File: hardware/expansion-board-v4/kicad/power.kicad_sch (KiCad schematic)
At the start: 40 parts, among them J9 MX1.25WT-2P BAT, SW3 TS24CA, U1 ME6211C33M5, U18 CH224K, U19 SY6970, U2 TPS7A2033PDBVR, U20 SY7069, U3 TPS7A2033PDBVR

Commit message: hardware(v4.7): 修正 C99 并刷新整套制造与装配文件
在用户修订的布局上将 C99 改为 100nF/0402，复用 C37/C52 的 C307331；同步原理图版本、BOM/CPL、装配图、安装助手及制造归档，更新下单入口和未决电气项。

验证：DRC 0 违规/0 未连通，存盘覆铜与包源一致性已核对；提交前版本包/安装助手20项，18通过、2跳过。元件契约中已记录的 C84 两条子断言失败按用户范围保留；Y4 供电和 U22 VREF 建议尚待闭环。内部工具、审计报告和采购过程文件按仓库规则仅留本地。
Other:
- title: Expansion Board V1 - Power: 5V in, 3x LDO -> Expansion Board V4.7 - Power: 5V in, 3x LDO
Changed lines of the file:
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@@
 	(paper "A3")
 	(title_block
-		(title "Expansion Board V1 - Power: 5V in, 3x LDO")
+		(title "Expansion Board V4.7 - Power: 5V in, 3x LDO")
 		(date "2026-08-01")
-		(rev "V1")
+		(rev "V4.7")
 		(company "Pilot Kit")
 	)

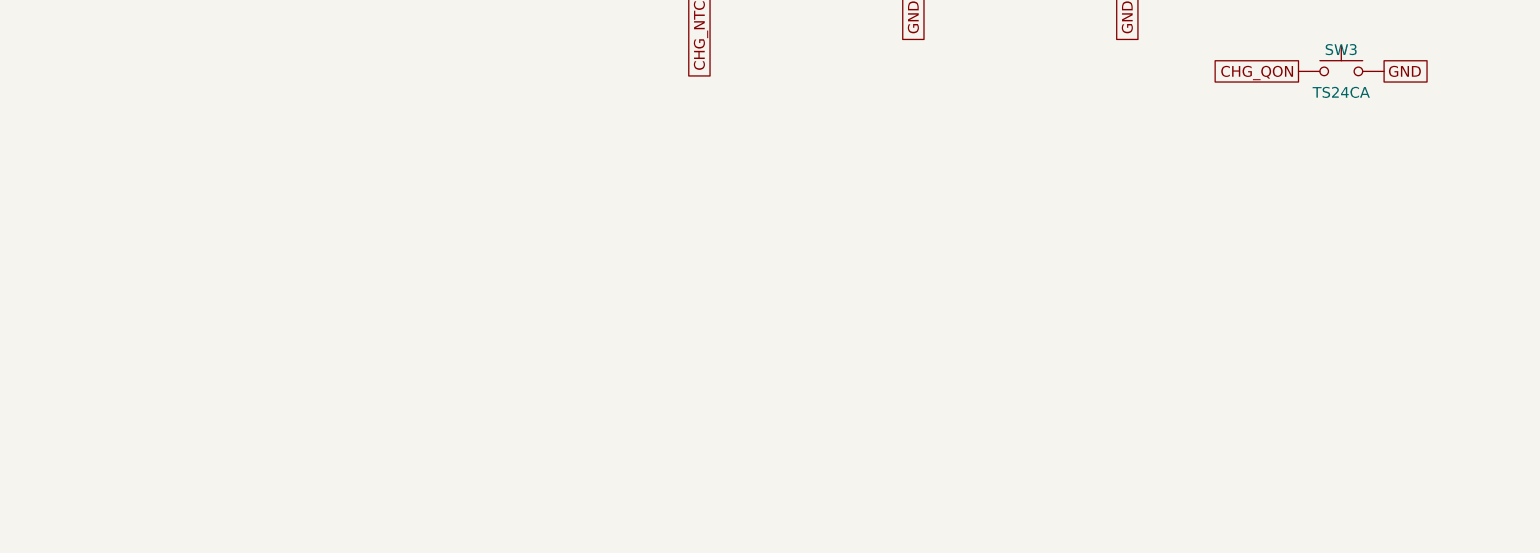
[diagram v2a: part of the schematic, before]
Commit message: hardware(v4.8): GNSS 模块 VBAT 常供电，开机不再冷启动
板上那颗 ATGM336H 本身就有 RTC（6N 手册 §2.4：pin6 VBAT = "RTC 及 SRAM 后备
电源"），但 pin6 一直接在 3V3_GNSS 上——与模块主供电同一条轨，关机
(BATFET_DIS) 时一起断电。于是模块每次开机都从零冷启动：既没有时间，也没有
星历。这同时是「开机没有时间」的硬件根因，和 gps_task.c 里 "gps-coarse" 粗校
兜底一直走不到的原因。

方案成立的前提先做了实机验证：室外定位后拔掉天线，让模块彻底失锁
(fix=0 sats=0 snr=0)，RMC 的时间字段仍逐秒前进 —— 模块的 RTC 确实独立于定位
在走。所以不需要外挂 RTC 芯片，板上已经有一颗，缺的只是一路不断电的 VBAT。

电路（6 件，取电点是 BAT_P：关机断的是 BAT→SYS，BAT_P 这侧照常带电）
    BAT_P ─[U23 TPS7A2033]─ 3V3_BKP ─[D7]─┬─ GNSS_VBAT ─ U7.pin6
                                          └─[R63 2.2k]─ BT1(+)
    C101/C102 = U23 的输入/输出去耦

  · U23 复用已采购料号 C2862740（BOM 用量 2→3），IGND 典型 6.5µA；
    加 GNSS 的 Ibat 10µA，总账约 17µA —— 对 5000mAh 是 33 年量级
  · D7 不能省：TPS7A20 手册写明输入掉电时电流会从 OUT 倒灌回 IN 并可能损坏
    器件。主电池被保护板切断后 BAT_P=0，没有它电池就会经 LDO 往回灌
  · BT1 = Seiko MS621FE-FL11E 焊接式可充电锂锰，5.5mAh，充到 2.91V 约 75%
    → 续航约 17 天。⚠️ 只能用 ML/MS 体系，**LIR 系列满电 4.2V 会超 Vbat 极限 3.6V**
  · 中途曾设计成「带线 CR2032 + 座子」（先 PH2.0 后 SH1.0），焊接式把座子和
    一颗 OR-ing 二极管一起省掉，"4.2V 主电池插错备份口"这条失效路径也随之消失

自建封装与 3D 模型（KiCad 官方库那个用不了）
  官方库有同名的 BatteryHolder_Seiko_MS621F，但它焊盘中心距 1.5mm，而
  FL11E 实际是 2.5mm，差 1mm 焊不上 —— 同一颗电池不同端子后缀
  （FL11E / FL01E / FE11E）焊脚并不通用，跟 J9 栽的是同一类坑。
  封装按 SII 官方样本 MicroBattery_E_20230330_rev05 第 14 页 1:1 建立。
  .wrl 里的圆柱必须用 IndexedFaceSet 显式建面：用 VRML 的 Cylinder 图元时
  整个元件都不显示（连焊脚的 Box 一起没），KiCad 静默忽略、不报错。

两个 DRC 抓不到的坑
  1) U7.pin6 改网络时必须连旧走线一起摘。焊盘改了网络而压在它上面的 4 段
     3V3_GNSS 铜不动，两个网络就被直接短在一起、二极管被旁路，而 DRC 只会
     报"未连通"不会报"短路"——它们确实是连着的。
  2) BT1 初版摆在 (142,107)，与 M2.5 安装孔 H4 实际重叠 2.39mm，DRC 全程
     0 违例：孔挂 F 面、电池在 B 面，按层查 courtyard 两边各自合规，但螺丝
     是贯穿的。重新求解时把四个贯穿孔一并当障碍，现落点 (140,76.4)，
     距投影区 +4.10 / 距板右边 +4.60 / 最近障碍 +14.26。

布线由用户手工完成并 review 通过：缺线 0 / 孤立断头铜 0 / 焊盘未接覆铜 0 /
铜层 DRC 0 / 丝印 DRC 0 / In1 参考面完整。BKP_CELL 走线 0.15mm 宽、68.9mm 长，
按 IPC-2221 载流约 0.6A 而实际电流 0.4mA，线阻 0.23Ω 相对串联的 R63=2.2k
占 0.01% —— 线宽不是约束，这条路的限流本来就由 R63 决定。

动了三处门禁（都说明理由）
  · test_board_revision_contract: 目标版本 V4.7 → V4.8（版本跟随）
  · test_v4_placement_contract / test_component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
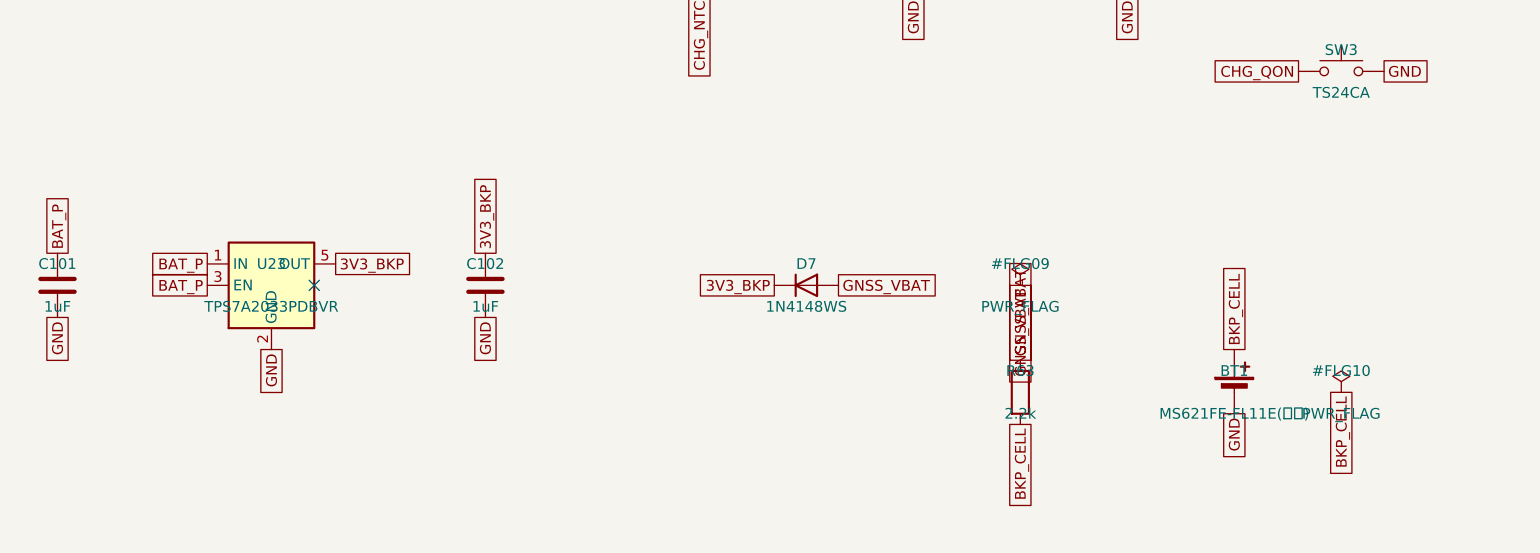
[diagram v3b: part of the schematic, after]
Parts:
- added BT1: MS621FE-FL11E(选贴), expansion-board-v4:MS621FE-FL11E, symbol Device:Battery_Cell
- added C101, C102: 1uF, Capacitor_SMD:C_0603_1608Metric, symbol Device:C
- added D7: 1N4148WS, Diode_SMD:D_SOD-323, symbol Device:D
- added R63: 2.2k, Resistor_SMD:R_0603_1608Metric, symbol Device:R
- added U23: TPS7A2033PDBVR, Package_TO_SOT_SMD:SOT-23-5, symbol Regulator_Linear:TPS7A20xxxDBV
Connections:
- net BAT_P: now also C101.1, U23.1 (IN), U23.3 (EN)
- net GND: now also BT1.2 (-), C101.2, C102.2, U23.2 (GND)
- new net 3V3_BKP: C102.1, D7.1 (K), U23.5 (OUT)
- new net BKP_CELL: BT1.1 (+), R63.2
- new net GNSS_VBAT: D7.2 (A), R63.1
- no-connect marks 9 -> 10
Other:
- title: Expansion Board V4.7 - Power: 5V in, 3x LDO -> Expansion Board V4.8 - Power: 5V in, 3x LDO

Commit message: hardware(v4.8): 修独立审计的 4 项，其中两项是设计错误
另一路 agent 的投产前独立审计报了 4 项，逐条核实**全部成立**，前两项是我的错。

① P1 — D7 极性接反（会让整条备份供电失效）
   KiCad 的 Device:D 符号是 **pin1=K(阴极) / pin2=A(阳极)**，我按"pin1 是阳极"
   的想当然写了 {"1":"3V3_BKP","2":"GNSS_VBAT"}，阳极落在了 GNSS_VBAT 侧。
   后果：U23 供不了电、BT1 充不上，而**DRC/ERC 都查不出极性方向**——网络连接
   完全"正确"，只是二极管装反了。注释里我写的明明是"阳极接 3V3_BKP"，落到
   代码时没去查符号定义。

   修法取了个巧：原理图交换引脚网络 + PCB 上 D7 旋转 180°。两个焊盘的物理位置
   随之互换，(80.874,88.324) 仍是 3V3_BKP、(80.874,86.224) 仍是 GNSS_VBAT，
   **走线一段都不用动**，而实物极性方向正过来了。

② P2 — BT1 焊盘中心距做成 2.5mm，官方是 1.5mm
   官方尺寸图标的是 `0.5 / 2 / 0.5`，那个 2 是**外缘到外缘**（1.5 中心距 +
   0.5 一条焊脚宽 = 2.0），我读成了内缘间距，于是算出 2.5。
   独立验算坐实：底视图按 φ6.8=472px 反算，两焊脚中心距 100px = 1.44mm、
   焊脚宽 36px = 0.52mm（官方标 0.5，比例尺自洽）。

   这也意味着**我当初否定 KiCad 官方封装的理由完全不成立**——它的 1.5mm 一直
   是对的。保留自建封装只是为了带自己的 3D 模型和这段记录，描述已改正。

   连带修掉的：3D 模型焊脚位置同步 ±1.25→±0.75；重放 BT1 时我漏了原朝向
   （-90°）导致焊盘跑到另一侧，补回后两条走线各差 0.5mm，已接上；焊盘移动后
   压到 GND 覆铜（clearance + solder_mask_bridge），重灌覆铜解决；丝印圆
   R3.65 压在焊盘开窗上，收到 R3.05（焊盘内缘 3.2 以内）；D7 位号旋转后与
   C101/U7.pad5 相撞，已重新安置。

③ P1 — 下单入口仍指向 V4.7
   release/README.md 标题、两个包链接、SHA256，以及 internal/下单说明.md 的
   四处引用，全部改指 V4.8 并重算校验值。照旧文档下单会拿到没有备份供电的板。

④ P2 — 选择性贴装规则未同步
   SELECTIVE_PLACEMENT 的「电源部分」名单漏了新增 6 件（中英文都漏），
   计数 29→35。**这是同一个陷阱第三次出现**：gen_assembly_web.py 的
   POWER_SECTION 上一轮刚补过，这次轮到手写文档。它们全部吊在 BAT_P 上，
   不带电源版不贴 U19/J9 时必须跟着不贴，否则 U23 输入悬空、整组失效而板子
   照常工作。

修复后板子状态
   缺线 0 / 孤立断头铜 0 / 焊盘未接覆铜 0
   铜层 DRC **0 违例** / 丝印 DRC **0 违例**
   走线 1849 段 / 过孔 492
   D7 电流方向 3V3_BKP → GNSS_VBAT ✓   BT1 焊盘中心距 1.50mm ✓

全部产物按修复后的板重出：ROUTES/PLACEMENT/ZONES/SILK、BOM、装配文档、
CHECKLIST、SMT 三变体、render、Gerber 与源码包（旧包留档在
build/pre-audit-fix-release/）、装配助手数据。

门禁：V4 全绿；遗留 4 项均为 expansion-board-v3 既存失败。
⚠️ check_gerber.py 仍未跑（缺 gerbonara），274X 格式与原点参数无替代验证。
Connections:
- net 3V3_BKP: now also D7.2 (A); no longer D7.1 (K)
- net GNSS_VBAT: now also D7.1 (K); no longer D7.2 (A)
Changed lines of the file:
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@@
 		)
 	)
-	(global_label "3V3_BKP"
+	(global_label "GNSS_VBAT"
 		(shape passive)
 		(at 135.89 241.3 180)
 		(effects (font (size 1.27 1.27)) (justify right))
 	)
-	(global_label "GNSS_VBAT"
+	(global_label "3V3_BKP"
 		(shape passive)
 		(at 143.51 241.3 0)

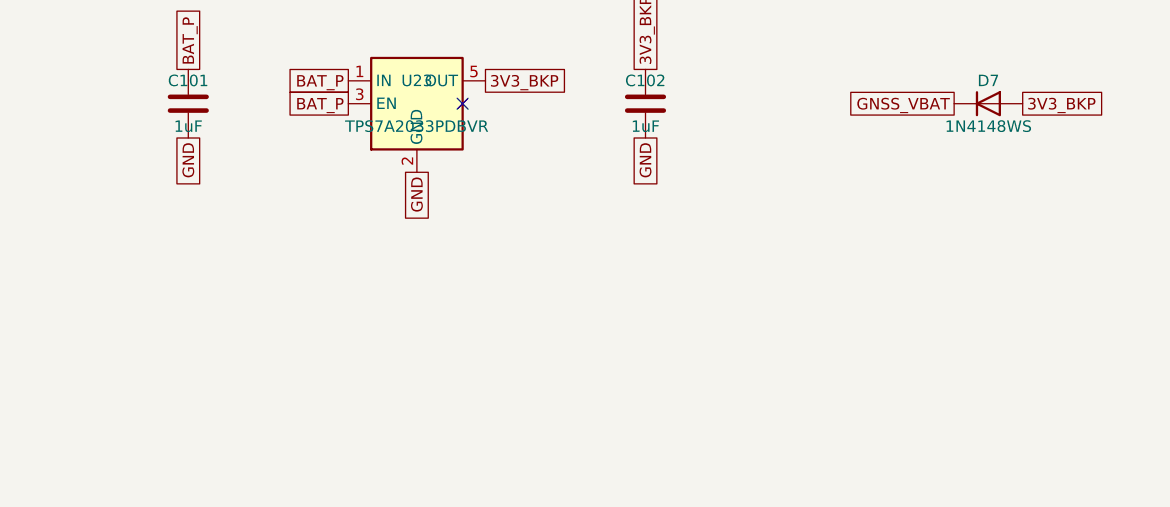
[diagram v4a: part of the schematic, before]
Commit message: hardware(v4.8): 加电源/充电指示灯 D8/D9，丝印回丝印层，电源选贴名单四处对齐
## 加了什么

全板此前**一颗 LED 都没有**（D2~D6 是 ESD 管、D7 是备份供电二极管），
上电后没有任何不拆机可见的状态。

    D8 + R64   电源灯   3V3_DIG → LED → 1k → GND，上电即亮、关机自灭
    D9 + R65   充电灯   3V3_DIG → LED → 1k → CHG_STAT

CHG_STAT 原本是条**死信号**：SY6970 的 STAT(pin4) 开漏输出 + R45 10k 上拉，
全板没有任何消费者。手册特性栏原文 "Charge Status Outputs for LED or Host"，
直驱 LED 就是设计用途。接上等于把它救活，且**不占任何 GPIO**——
充电中亮（STAT ≤0.4V）、充满灭（高阻被 R45 拉到 3V3，两端无压差）、
**充电故障 1Hz 闪**（手册原文，白捡一个故障指示）。

限流都用 1k 复用板上已有料号，不新增 SMT 上料种类；取 ~1mA 而非额定 20mA。

⚠️ 只能用 **Vf 2.0~2.2V** 档（红/黄/橙/普绿）。维护者那批样品包里的
蓝(467-470nm)、翠绿(520-523)、白 是 **3.0~3.1V**，挂 3.3V 轨上点不亮——
充电灯还要再扣 STAT 的 0.4V，只剩 0.2V，连正向导通都不够。
所以 value 锁 Vf 档不锁颜色，颜色手焊时挑。D8/D9 自备料、无嘉立创料号，
和 BT1 一样不进任何 CPL，需手焊。

## 丝印：位号一律留丝印层（维护者纠正）

我一度把 D8/D9/R64/R65/SW3 五个位号搬到 **F.Fab** 来消除 14 项丝印 DRC 违例。
维护者纠正：「你又把丝印放到 FFAB 了，**每次都这样**」。

搬 F.Fab 不是解决问题，是**把问题藏起来**——板面丝印是实物上唯一能直接读到
的位号，手焊/返修/现场排查都靠它，F.Fab 只存在于装配图 PDF 里。
当时那三条自辩全部不成立：维护者自己在 KiCad 里重排了一遍，五个位号
**全部回到 F.Silkscreen、字高 0.8mm，丝印 DRC 依然 0 违例**。

连带损失也暴露了：export_placement **只冻结丝印层的位号**（F.Fab 被它判为
"算法排不下"的失败状态，不予固化），所以那 5 个当场丢掉固化，
PLACEMENT.py 报「240 元件 / **235** 位号」。改回来后恢复 240/240。

维护者还加了两条板级功能标注 `PWR↓` / `CHG↓`（F.SilkS 0.8mm，箭头各指一灯）
——位号只说"这是个二极管"，这两条才说明它是干什么的。
门禁按 test_v4_placement_contract 自己的设计**单列** V48_LABELS，
没有把 FINALIZED_GRAPHICS_COUNT 基线 +1（那会让合同退化成事后追认）；
已做突变验证：数错一条会变红。

## 电源选贴名单：四处副本对齐

D9/R65 的阴极落在 U19 的 STAT 脚上，不带电源版没有 U19 就永远不亮，
必须随电源部分一起不贴。D8/R64 吃 3V3_DIG（U1 从 VCC_5V 降压），
两个版本都要贴，**不在此列**。

补登时发现这份名单在仓库里有**四处**同语义副本，而 2026-09-13 加 GNSS
备份供电那 6 件时**只登记了一处**：

    tools/gen_assembly_web.py           POWER_SECTION  ← 当时只改了这处
    internal/tools/gen_jlc_smt.py       VARIANT_PWR    ← 漏
    internal/tools/gen_assembly_pdf.py  VARIANT_PWR    ← 漏
    internal/tools/gen_place_xlsx.py    PWR_REFS       ← 漏

没暴露只因为 BUILD_VARIANT 一直是 "powered"，VARIANT_PWR 压根没参与计算。
四处现已一致（各 37 个位号，脚本核对过），并在每处写明另外三处在哪、
以及哪两处（gen_power_csv.WANT 采购口径 / gen_pcb.BACKSIDE B面集合）
语义不同不要跟着改。装配图的「电源区」随之从 29 → 37。

## 布线与丝印上踩到的

· 0805 竖放 c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
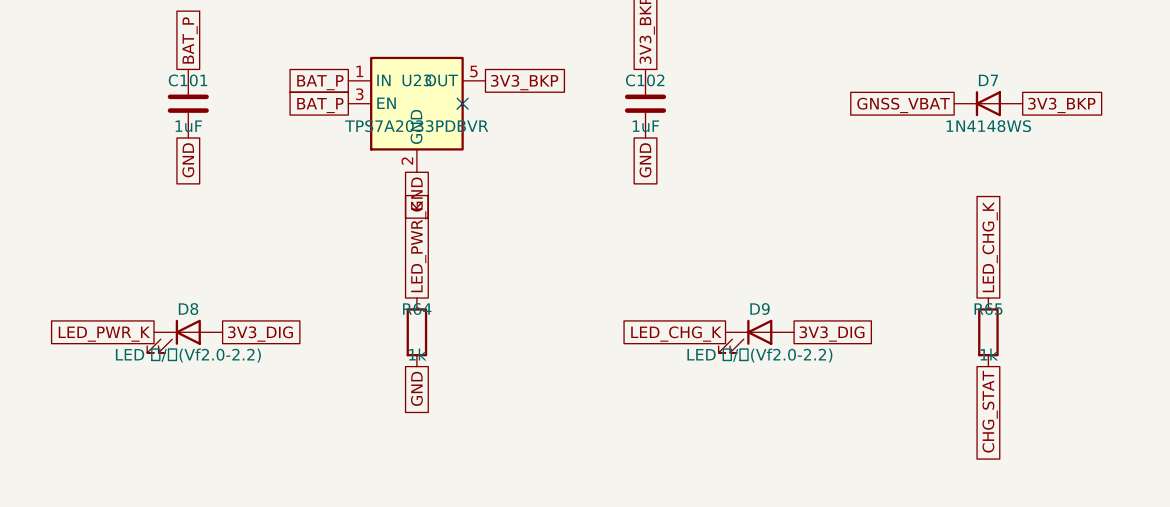
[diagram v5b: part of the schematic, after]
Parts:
- added D8, D9: LED 红/黄(Vf2.0-2.2), LED_SMD:LED_0805_2012Metric, symbol Device:LED
- added R64, R65: 1k, Resistor_SMD:R_0603_1608Metric, symbol Device:R
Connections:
- net 3V3_DIG: now also D8.2 (A), D9.2 (A)
- net CHG_STAT: now also R65.2
- net GND: now also R64.2
- new net LED_CHG_K: D9.1 (K), R65.1
- new net LED_PWR_K: D8.1 (K), R64.1
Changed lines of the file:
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@@
+		(effects (font (size 1.27 1.27)) (justify right))
+	)
+	(symbol
+		(lib_id "Device:LED")
+		(at 50.8 266.7 0)
+		(unit 1)
+		(exclude_from_sim no)
+		(in_bom yes)
+		(on_board yes)
+		(dnp no)
+		(property "Reference" "D8"
+			(at 50.8 264.16 0)
+			(effects (font (size 1.27 1.27)))
+		)
+		(property "Value" "LED 红/黄(Vf2.0-2.2)"
+			(at 50.8 269.24 0)
+			(effects (font (size 1.27 1.27)))
+		)
+		(property "Footprint" "LED_SMD:LED_0805_2012Metric"
+			(at 50.8 271.78 0)
+			(effects (font (size 1.27 1.27))
+				(hide yes))
+		)
+		(property "Datasheet" "~"
+			(at 50.8 274.32 0)
+			(effects (font (size 1.27 1.27))
+				(hide yes))
+		)
+		(pin "1"
+		)
+		(pin "2"
+		)
+		(instances
+			(project "expansion-board-v4"
+				(path "/10000000-0000-4000-8000-000000000001/20000000-0000-4000-8000-000000000001"
+					(reference "D8")
+					(unit 1)
+				)
+			)
+		)
+	)
+	(global_label "LED_PWR_K"
+		(shape passive)
+		(at 46.99 266.7 180)
+		(effects (font (size 1.27 1.27)) (justify right))
+	)
+	(global_label "3V3_DIG"
+		(shape passive)
+		(at 54.61 266.7 0)
+		(effects (font (size 1.27 1.27)) (justify left))
+	)
+	(symbol
+		(lib_id "Device:R")
+		(at 76.2 266.7 0)
+		(unit 1)
+		(exclude_from_sim no)
+		(in_bom yes)
+		(on_board yes)
+		(dnp no)
+		(property "Reference" "R64"
+			(at 76.2 264.16 0)
+			(effects (font (size 1.27 1.27)))
+		)
+		(property "Value" "1k"
+			(at 76.2 269.24 0)
+			(effects (font (size 1.27 1.27)))
+		)
+		(property "Footprint" "Resistor_SMD:R_0603_1608Metric"
+			(at 76.2 271.78 0)
+			(effects (font (size 1.27 1.27))
+				(hide yes))
+		)
+		(property "Datasheet" "~"
+			(at 76.2 274.32 0)
+			(effects (font (size 1.27 1.27))
+				(hide yes))
+		)
+		(pin "1"
+		)
+		(pin "2"
+		)
+		(instances
+			(project "expansion-board-v4"
+				(path "/10000000-0000-4000-8000-000000000001/20000000-0000-4000-8000-000000000001"
+					(reference "R64")
+					(unit 1)
+				)
+			)
+		)
+	)
+	(global_label "LED_PWR_K"
+		(shape passive)
+		(at 76.2 262.89 270)
+		(effects (font (size 1.27 1.27)) (justify left))
+	)
+	(global_label "GND"
+		(shape passive)
+		(at 76.2 270.51 90)
+		(effects (font (size 1.27 1.27)) (justify right))
+	)
+	(symbol
+		(lib_id "Device:LED")
+		(at 114.3 266.7 0)
+		(unit 1)
+		(exclude_from_sim no)
+		(in_bom yes)
+		(on_board yes)
+		(dnp no)
+		(property "Reference" "D9"
+			(at 114.3 264.16 0)
+			(effects (font (size 1.27 1.27)))
+		)
+		(property "Value" "LED 红/黄(Vf2.0-2.2)"
+			(at 114.3 269.24 0)
+			(effects (font (size 1.27 1.27)))
+		)
+		(property "Footprint" "LED_SMD:LED_0805_2012Metric"
+			(at 114.3 271.78 0)
+			(effects (font (size 1.27 1.27))
+				(hide yes))
+		)
+		(property "Datasheet" "~"
+			(at 114.3 274.32 0)
+			(effects (font (size 1.27 1.27))
+				(hide yes))
+		)
+		(pin "1"
+		)
+		(pin "2"
+		)
+		(instances
+			(project "expansion-board-v4"
+				(path "/10000000-0000-4000-8000-000000000001/20000000-0000-4000-8000-000000000001"
+					(reference "D9")
+					(unit 1)
+				)
+			)
+		)
+	)
+	(global_label "LED_CHG_K"
+		(shape passive)
+		(at 110.49 266.7 180)
+		(effects (font (size 1.27 1.27)) (justify right))
+	)
+	(global_label "3V3_DIG"
+		(shape passive)
+		(at 118.11 266.7 0)
+		(effects (font (size 1.27 1.27)) (justify left))
+	)
+	(symbol
+		(lib_id "Device:R")
+		(at 139.7 266.7 0)
+		(unit 1)
+		(exclude_from_sim no)
+		(in_bom yes)
+		(on_board yes)
+		(dnp no)
+		(property "Reference" "R65"
+			(at 139.7 264.16 0)
+			(effects (font (size 1.27 1.27)))
+		)
+		(property "Value" "1k"
+			(at 139.7 269.24 0)
+			(effects (font (size 1.27 1.27)))
+		)
+		(property "Footprint" "Resistor_SMD:R_0603_1608Metric"
+			(at 139.7 271.78 0)
+			(effects (font (size 1.27 1.27))
+				(hide yes))
+		)
+		(property "Datasheet" "~"
+			(at 139.7 274.32 0)
+			(effects (font (size 1.27 1.27))
+				(hide yes))
+		)
+		(pin "1"
+		)
+		(pin "2"
+		)
+		(instances
+			(project "expansion-board-v4"
+				(path "/10000000-0000-4000-8000-000000000001/20000000-0000-4000-8000-000000000001"
+					(reference "R65")
+					(unit 1)
+				)
+			)
+		)
+	)
+	(global_label "LED_CHG_K"
+		(shape passive)
+		(at 139.7 262.89 270)
+		(effects (font (size 1.27 1.27)) (justify left))
+	)
+	(global_label "CHG_STAT"
+		(shape passive)
+		(at 139.7 270.51 90)
 		(effects (font (size 1.27 1.27)) (justify right))
 	)

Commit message: feat(v4.11): 固化扩展板并修正电池补偿
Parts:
- added D10: 1N4148WS, Diode_SMD:D_SOD-323, symbol Device:D
- added R67: 1k, Resistor_SMD:R_0603_1608Metric, symbol Device:R
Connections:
- net CHG_QON: now also D10.1 (K)
- new net P4_GPIO4_SW3_SENSE: R67.1
- new net SW3_SENSE_A: D10.2 (A), R67.2
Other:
- title: Expansion Board V4.8 - Power: 5V in, 3x LDO -> Expansion Board V4.11 - Power: 5V in, 3x LDO
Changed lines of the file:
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@@
 	(paper "A3")
 	(title_block
-		(title "Expansion Board V4.8 - Power: 5V in, 3x LDO")
+		(title "Expansion Board V4.11 - Power: 5V in, 3x LDO")
 		(date "2026-08-01")
-		(rev "V4.8")
+		(rev "V4.11")
 		(company "Pilot Kit")
 	)
@@
 		(effects (font (size 1.27 1.27)) (justify left))
 	)
+	(symbol
+		(lib_id "Device:R")
+		(at 228.6 215.9 0)
+		(unit 1)
+		(exclude_from_sim no)
+		(in_bom yes)
+		(on_board yes)
+		(dnp no)
+		(property "Reference" "R67"
+			(at 228.6 213.36 0)
+			(effects (font (size 1.27 1.27)))
+		)
+		(property "Value" "1k"
+			(at 228.6 218.44 0)
+			(effects (font (size 1.27 1.27)))
+		)
+		(property "Footprint" "Resistor_SMD:R_0603_1608Metric"
+			(at 228.6 220.98 0)
+			(effects (font (size 1.27 1.27))
+				(hide yes))
+		)
+		(property "Datasheet" "~"
+			(at 228.6 223.52 0)
+			(effects (font (size 1.27 1.27))
+				(hide yes))
+		)
+		(pin "1"
+		)
+		(pin "2"
+		)
+		(instances
+			(project "expansion-board-v4"
+				(path "/10000000-0000-4000-8000-000000000001/20000000-0000-4000-8000-000000000001"
+					(reference "R67")
+					(unit 1)
+				)
+			)
+		)
+	)
+	(global_label "P4_GPIO4_SW3_SENSE"
+		(shape passive)
+		(at 228.6 212.09 270)
+		(effects (font (size 1.27 1.27)) (justify left))
+	)
+	(global_label "SW3_SENSE_A"
+		(shape passive)
+		(at 228.6 219.71 90)
+		(effects (font (size 1.27 1.27)) (justify right))
+	)
+	(symbol
+		(lib_id "Device:D")
+		(at 254 215.9 0)
+		(unit 1)
+		(exclude_from_sim no)
+		(in_bom yes)
+		(on_board yes)
+		(dnp no)
+		(property "Reference" "D10"
+			(at 254 213.36 0)
+			(effects (font (size 1.27 1.27)))
+		)
+		(property "Value" "1N4148WS"
+			(at 254 218.44 0)
+			(effects (font (size 1.27 1.27)))
+		)
+		(property "Footprint" "Diode_SMD:D_SOD-323"
+			(at 254 220.98 0)
+			(effects (font (size 1.27 1.27))
+				(hide yes))
+		)
+		(property "Datasheet" "~"
+			(at 254 223.52 0)
+			(effects (font (size 1.27 1.27))
+				(hide yes))
+		)
+		(pin "1"
+		)
+		(pin "2"
+		)
+		(instances
+			(project "expansion-board-v4"
+				(path "/10000000-0000-4000-8000-000000000001/20000000-0000-4000-8000-000000000001"
+					(reference "D10")
+					(unit 1)
+				)
+			)
+		)
+	)
+	(global_label "CHG_QON"
+		(shape passive)
+		(at 250.19 215.9 180)
+		(effects (font (size 1.27 1.27)) (justify right))
+	)
+	(global_label "SW3_SENSE_A"
+		(shape passive)
+		(at 257.81 215.9 0)
+		(effects (font (size 1.27 1.27)) (justify left))
+	)
